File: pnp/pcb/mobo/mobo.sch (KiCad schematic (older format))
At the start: 21 parts, among them J5 Conn_ARM_JTAG_SWD_10, SW2 RESET, U1 STM32F407VETx, Y1 12MHz, Y3 32.768MHz

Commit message: decided to stick with original layout. added footprint and schematic for 2SMPP-03 vacuum sensor
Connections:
- net labels removed: MOTOR_CIPO, MOTOR_COPI, MOTOR_C_CS, MOTOR_P_CS, MOTOR_R_CS, MOTOR_SCK, MOTOR_X_CS, MOTOR_Y_CS, MOTOR_Z_CS
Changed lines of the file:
@@
 Text GLabel 2200 6600 0    50   Input ~ 0
 485_3_RTS
-Text GLabel 4000 6500 2    50   Input ~ 0
-MOTOR_CIPO
-Text GLabel 4000 6600 2    50   Input ~ 0
-MOTOR_COPI
-Text GLabel 4000 6400 2    50   Input ~ 0
-MOTOR_SCK
-Text GLabel 4000 3500 2    50   Input ~ 0
-MOTOR_X_CS
-Text GLabel 4000 4500 2    50   Input ~ 0
-MOTOR_Y_CS
-Text GLabel 4000 4600 2    50   Input ~ 0
-MOTOR_Z_CS
-Text GLabel 4000 5800 2    50   Input ~ 0
-MOTOR_R_CS
-Text GLabel 4000 5900 2    50   Input ~ 0
-MOTOR_P_CS
-Text GLabel 4000 6000 2    50   Input ~ 0
-MOTOR_C_CS
 $Comp
 L Device:R_Small R1

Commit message: reassigned gpio to make routing easier, did some routing, started working out the schematic for the 2smpp-03
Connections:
- net labels added: C_LIMIT, P_LIMIT, R_LIMIT
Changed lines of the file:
@@
 Text Notes 7000 6650 0    50   ~ 0
 Therm3 -> VAC1\n
-Text GLabel 2200 6100 0    50   Input ~ 0
+Text GLabel 2200 4200 0    50   Input ~ 0
 Z_DIR
-Text GLabel 2200 6000 0    50   Input ~ 0
+Text GLabel 2200 4300 0    50   Input ~ 0
 Z_STEP
-Text GLabel 2200 5800 0    50   Input ~ 0
+Text GLabel 4000 6700 2    50   Input ~ 0
 Z_EN
 Text GLabel 4000 5400 2    50   Input ~ 0
 VAC1_SIG
-Text GLabel 2200 3800 0    50   Input ~ 0
+Text GLabel 2200 6800 0    50   Input ~ 0
 Y_LIMIT
+Text GLabel 4000 4900 2    50   Input ~ 0
+MOSFET4_EN
 Text GLabel 4000 5200 2    50   Input ~ 0
-MOSFET4_EN
-Text GLabel 4000 4900 2    50   Input ~ 0
 MOSFET1_EN
-Text GLabel 4000 5000 2    50   Input ~ 0
+Text GLabel 4000 5100 2    50   Input ~ 0
 MOSFET2_EN
-Text GLabel 2200 4900 0    50   Input ~ 0
+Text GLabel 2200 4800 0    50   Input ~ 0
 SERVO1_SIG
-Text GLabel 2200 4700 0    50   Input ~ 0
+Text GLabel 2200 5400 0    50   Input ~ 0
 Y_DIR
-Text GLabel 2200 4800 0    50   Input ~ 0
+Text GLabel 2200 5500 0    50   Input ~ 0
 Y_STEP
 Text GLabel 4000 5700 2    50   Input ~ 0
@@
 Text GLabel 4000 5500 2    50   Input ~ 0
 VAC2_SIG
-Text GLabel 2200 5000 0    50   Input ~ 0
+Text GLabel 2200 5600 0    50   Input ~ 0
 Y_EN
-Text GLabel 2200 5600 0    50   Input ~ 0
+Text GLabel 2200 6000 0    50   Input ~ 0
 X_DIR
-Text GLabel 2200 5700 0    50   Input ~ 0
+Text GLabel 2200 6100 0    50   Input ~ 0
 X_STEP
-Text GLabel 2200 3700 0    50   Input ~ 0
+Text GLabel 4000 6000 2    50   Input ~ 0
 X_LIMIT
-Text GLabel 2200 6800 0    50   Input ~ 0
+Text GLabel 2200 5800 0    50   Input ~ 0
 C_STEP
-Text GLabel 2200 5200 0    50   Input ~ 0
+Text GLabel 2200 4900 0    50   Input ~ 0
 SERVO2_SIG
-Text GLabel 2200 5400 0    50   Input ~ 0
+Text GLabel 4000 4000 2    50   Input ~ 0
 X_EN
-Text GLabel 2200 5100 0    50   Input ~ 0
+Text GLabel 4000 6300 2    50   Input ~ 0
 Z_LIMIT
 Text GLabel 4000 4800 2    50   Input ~ 0
@@
 Text GLabel 4000 4700 2    50   Input ~ 0
 SCL
-Text GLabel 2200 4000 0    50   Input ~ 0
+Text GLabel 4000 4300 2    50   Input ~ 0
 P_EN
-Text GLabel 2200 4300 0    50   Input ~ 0
+Text GLabel 2200 5000 0    50   Input ~ 0
 DOWNWARDS_LIGHT_SIG
-Text GLabel 2200 4200 0    50   Input ~ 0
+Text GLabel 2200 5100 0    50   Input ~ 0
 UPWARDS_LIGHT_SIG
-Text GLabel 2200 3900 0    50   Input ~ 0
+Text GLabel 4000 4100 2    50   Input ~ 0
 P_DIR
-Text GLabel 2200 6900 0    50   Input ~ 0
+Text GLabel 2200 5700 0    50   Input ~ 0
 C_DIR
-Text GLabel 2200 4100 0    50   Input ~ 0
+Text GLabel 4000 4200 2    50   Input ~ 0
 P_STEP
-Text GLabel 2200 6700 0    50   Input ~ 0
+Text GLabel 2200 5900 0    50   Input ~ 0
 C_EN
-Text GLabel 4000 5100 2    50   Input ~ 0
+Text GLabel 4000 5000 2    50   Input ~ 0
 MOSFET3_EN
 Text GLabel 4000 2600 2    50   Input ~ 0
@@
 Text GLabel 4000 2500 2    50   Input ~ 0
 SCK
-Text GLabel 4000 4300 2    50   Input ~ 0
+Text GLabel 2200 3900 0    50   Input ~ 0
 R_DIR
-Text GLabel 4000 4200 2    50   Input ~ 0
+Text GLabel 2200 4000 0    50   Input ~ 0
 R_STEP
-Text GLabel 4000 4000 2    50   Input ~ 0
+Text GLabel 2200 4100 0    50   Input ~ 0
 R_EN
 $Comp
@@
 Wire Wire Line
 	900  3750 900  3800
+Text GLabel 4000 6200 2    50   Input ~ 0
+R_LIMIT
+Text GLabel 4000 6100 2    50   Input ~ 0
+P_LIMIT
+Text GLabel 2200 6900 0    50   Input ~ 0
+C_LIMIT
 $EndSCHEMATC

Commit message: finished schematics for vacuum sensor, did some more routing for mosfets
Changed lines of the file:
@@
 Text GLabel 4000 5400 2    50   Input ~ 0
 VAC1_SIG
-Text GLabel 2200 6800 0    50   Input ~ 0
+Text GLabel 4000 5000 2    50   Input ~ 0
 Y_LIMIT
-Text GLabel 4000 4900 2    50   Input ~ 0
+Text GLabel 2200 6700 0    50   Input ~ 0
 MOSFET4_EN
-Text GLabel 4000 5200 2    50   Input ~ 0
+Text GLabel 4000 6000 2    50   Input ~ 0
 MOSFET1_EN
-Text GLabel 4000 5100 2    50   Input ~ 0
+Text GLabel 2200 6900 0    50   Input ~ 0
 MOSFET2_EN
 Text GLabel 2200 4800 0    50   Input ~ 0
@@
 Text GLabel 2200 6100 0    50   Input ~ 0
 X_STEP
-Text GLabel 4000 6000 2    50   Input ~ 0
+Text GLabel 4000 5200 2    50   Input ~ 0
 X_LIMIT
 Text GLabel 2200 5800 0    50   Input ~ 0
@@
 Text GLabel 2200 5900 0    50   Input ~ 0
 C_EN
-Text GLabel 4000 5000 2    50   Input ~ 0
+Text GLabel 2200 6800 0    50   Input ~ 0
 MOSFET3_EN
 Text GLabel 4000 2600 2    50   Input ~ 0
@@
 Wire Wire Line
 	2200 2850 2250 2850
-Text GLabel 4000 2900 2    50   Input ~ 0
+Text GLabel 2200 6200 0    50   Input ~ 0
 485_1_RXI
-Text GLabel 4000 3000 2    50   Input ~ 0
+Text GLabel 2200 6300 0    50   Input ~ 0
 485_1_TXO
-Text GLabel 4000 2800 2    50   Input ~ 0
+Text GLabel 2200 6600 0    50   Input ~ 0
 485_1_RTS
 Text GLabel 4000 2200 2    50   Input ~ 0
@@
 Text GLabel 4000 2100 2    50   Input ~ 0
 485_2_RTS
-Text GLabel 2200 6200 0    50   Input ~ 0
+Text GLabel 4000 2900 2    50   Input ~ 0
 485_3_RXI
-Text GLabel 2200 6300 0    50   Input ~ 0
+Text GLabel 4000 3000 2    50   Input ~ 0
 485_3_TXO
-Text GLabel 2200 6600 0    50   Input ~ 0
+Text GLabel 4000 2800 2    50   Input ~ 0
 485_3_RTS
 $Comp
@@
 Text GLabel 4000 6100 2    50   Input ~ 0
 P_LIMIT
-Text GLabel 2200 6900 0    50   Input ~ 0
+Text GLabel 4000 5100 2    50   Input ~ 0
 C_LIMIT
 $EndSCHEMATC

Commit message: cleaned up silkscreens, added version and info text
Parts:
- Y1: symbol Device:Crystal_GND24_Small -> mobo-rescue:Crystal_GND24_Small-Device
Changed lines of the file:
@@
 	5900 2500 5900 2450
 $Comp
-L Device:Crystal_GND24_Small Y1
+L mobo-rescue:Crystal_GND24_Small-Device Y1
 U 1 1 5F20EB5B
 P 900 3600

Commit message: switched to more monolithic vacuum sensor. rerouted for it. routed aux ports. exported and ordered. this commit exactly reflects REV001 hardware.
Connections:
- net labels added: AUX1-A1, AUX1-A2, AUX1-D1, AUX1-D2, AUX2-A1, AUX2-A2, AUX2-D1, AUX2-D2
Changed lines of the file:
@@
 Text GLabel 4000 5100 2    50   Input ~ 0
 C_LIMIT
+Text GLabel 4000 5800 2    50   Input ~ 0
+AUX1-A2
+Text GLabel 4000 5900 2    50   Input ~ 0
+AUX2-A2
+Text GLabel 2200 4600 0    50   Input ~ 0
+AUX1-D1
+Text GLabel 2200 4400 0    50   Input ~ 0
+AUX1-D2
+Text GLabel 2200 4700 0    50   Input ~ 0
+AUX2-D1
+Text GLabel 2200 4500 0    50   Input ~ 0
+AUX2-D2
+Text GLabel 4000 3800 2    50   Input ~ 0
+AUX2-A1
+Text GLabel 4000 3700 2    50   Input ~ 0
+AUX1-A1
 $EndSCHEMATC

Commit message: removed LSE and changed HSE to 8MHz
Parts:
- removed C23, C25: 22pF, Capacitor_SMD:C_0805_2012Metric_Pad1.15x1.40mm_HandSolder, symbol Device:C_Small
- removed Y3: 32.768MHz, Crystal:Crystal_SMD_3215-2Pin_3.2x1.5mm, symbol Device:Crystal_Small
- Y1: value 12MHz -> 8MHz
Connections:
- wire segments 74 -> 64
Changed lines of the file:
@@
 	1850 2750 1850 2700
-$Comp
-L Device:Crystal_Small Y3
-U 1 1 5F0E266F
-P 4400 7050
-F 0 "Y3" H 4400 7275 50  0000 C CNN
-F 1 "32.768MHz" H 4400 7184 50  0000 C CNN
-F 2 "Crystal:Crystal_SMD_3215-2Pin_3.2x1.5mm" H 4400 7050 50  0001 C CNN
-F 3 "~" H 4400 7050 50  0001 C CNN
-	1    4400 7050
-	1    0    0    -1
-$EndComp
-$Comp
-L Device:C_Small C25
-U 1 1 5F0E33A4
-P 4600 7250
-F 0 "C25" H 4692 7296 50  0000 L CNN
-F 1 "22pF" H 4692 7205 50  0000 L CNN
-F 2 "Capacitor_SMD:C_0805_2012Metric_Pad1.15x1.40mm_HandSolder" H 4600 7250 50  0001 C CNN
-F 3 "~" H 4600 7250 50  0001 C CNN
-	1    4600 7250
-	1    0    0    -1
-$EndComp
-$Comp
-L Device:C_Small C23
-U 1 1 5F0E4761
-P 4200 7250
-F 0 "C23" H 4292 7296 50  0000 L CNN
-F 1 "22pF" H 4292 7205 50  0000 L CNN
-F 2 "Capacitor_SMD:C_0805_2012Metric_Pad1.15x1.40mm_HandSolder" H 4200 7250 50  0001 C CNN
-F 3 "~" H 4200 7250 50  0001 C CNN
-	1    4200 7250
-	1    0    0    -1
-$EndComp
-Wire Wire Line
-	4200 7150 4200 7050
-Wire Wire Line
-	4200 7050 4300 7050
-Wire Wire Line
-	4500 7050 4600 7050
-Wire Wire Line
-	4600 7050 4600 7150
-$Comp
-L power:GND #PWR0124
-U 1 1 5F0E65D5
-P 4200 7450
-F 0 "#PWR0124" H 4200 7200 50  0001 C CNN
-F 1 "GND" H 4205 7277 50  0000 C CNN
-F 2 "" H 4200 7450 50  0001 C CNN
-F 3 "" H 4200 7450 50  0001 C CNN
-	1    4200 7450
-	1    0    0    -1
-$EndComp
-$Comp
-L power:GND #PWR0125
-U 1 1 5F0E6A2C
-P 4600 7450
-F 0 "#PWR0125" H 4600 7200 50  0001 C CNN
-F 1 "GND" H 4605 7277 50  0000 C CNN
-F 2 "" H 4600 7450 50  0001 C CNN
-F 3 "" H 4600 7450 50  0001 C CNN
-	1    4600 7450
-	1    0    0    -1
-$EndComp
-Wire Wire Line
-	4600 7450 4600 7350
-Wire Wire Line
-	4200 7450 4200 7350
-Wire Wire Line
-	4200 7050 4200 6900
-Wire Wire Line
-	4200 6900 4000 6900
-Connection ~ 4200 7050
-Wire Wire Line
-	4600 7050 4600 6800
-Wire Wire Line
-	4600 6800 4000 6800
-Connection ~ 4600 7050
 $Comp
 L Device:C_Small C15
@@
 P 900 3600
 F 0 "Y1" H 1044 3646 50  0000 L CNN
-F 1 "12MHz" H 750 3750 50  0000 L CNN
+F 1 "8MHz" H 750 3750 50  0000 L CNN
 F 2 "Crystal:Crystal_SMD_3225-4Pin_3.2x2.5mm" H 900 3600 50  0001 C CNN
 F 3 "~" H 900 3600 50  0001 C CNN

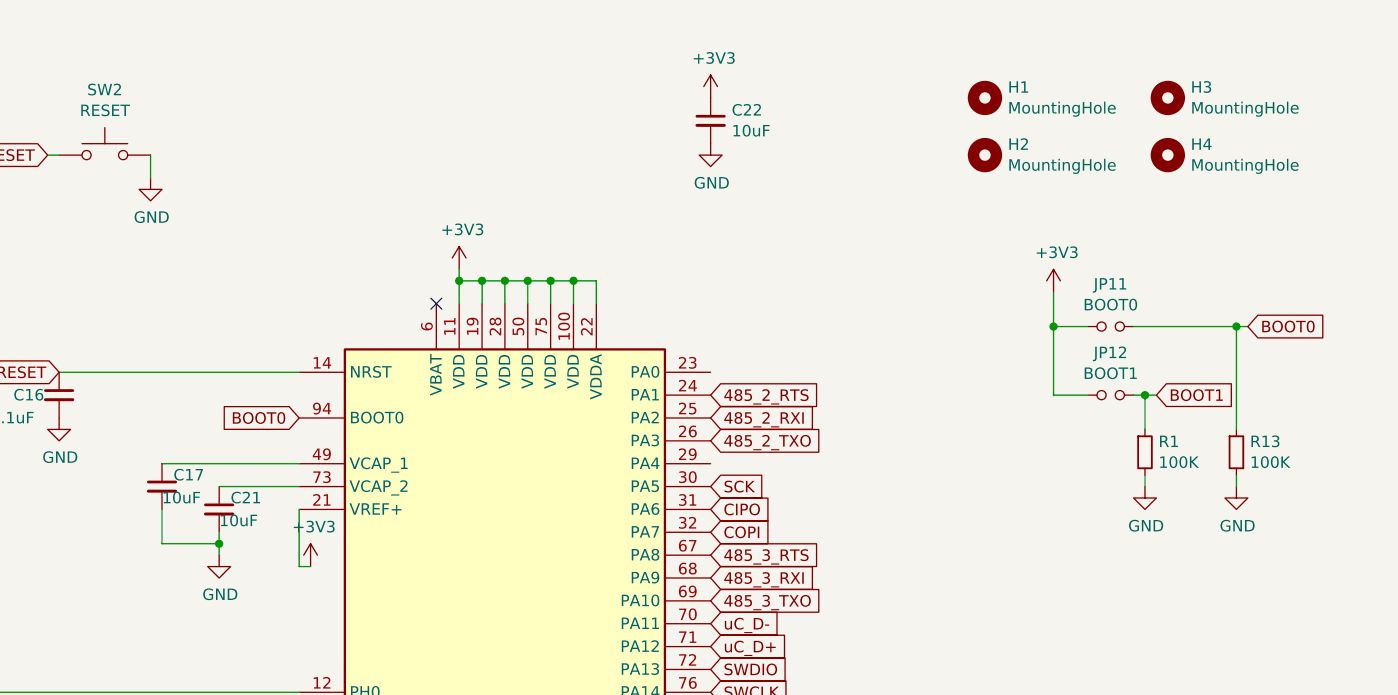
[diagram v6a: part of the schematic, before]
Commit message: fixing decoupling caps based on datasheet and reference design
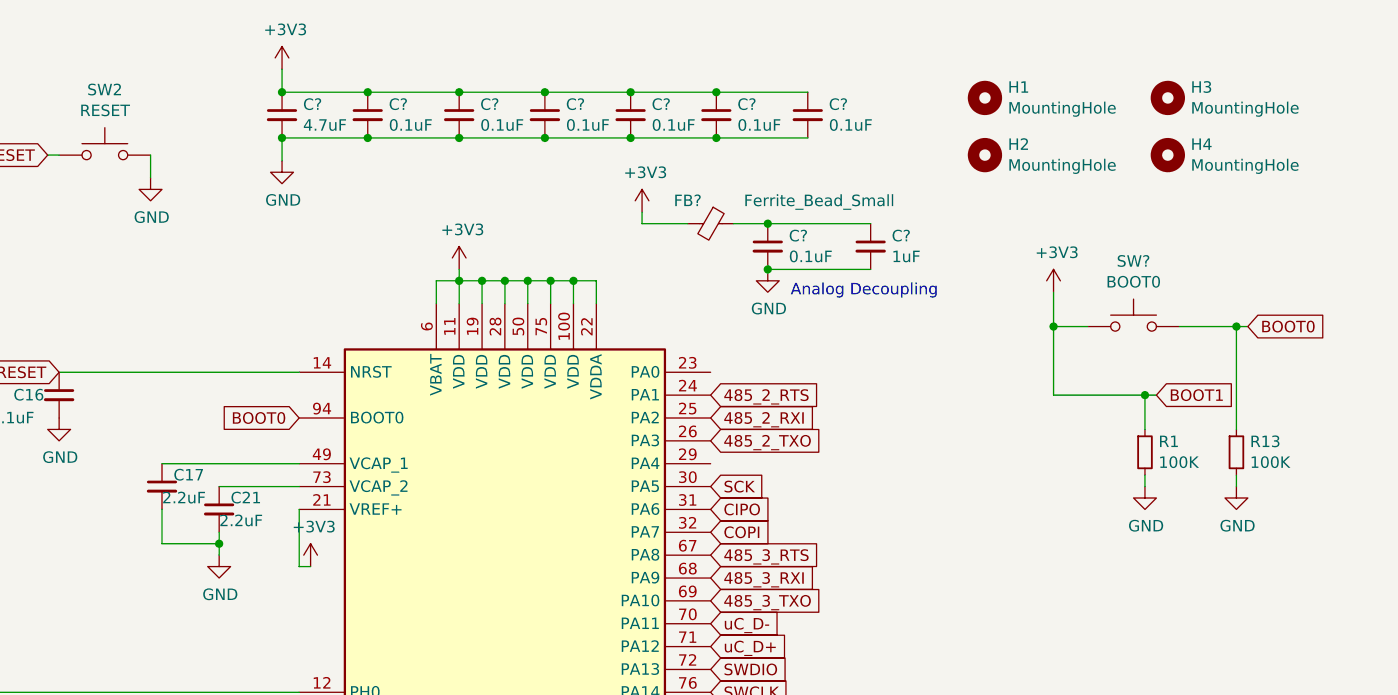
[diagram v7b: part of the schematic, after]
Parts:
- removed C22: 10uF, Capacitor_SMD:C_0805_2012Metric_Pad1.15x1.40mm_HandSolder, symbol Device:C_Small
- removed JP11: BOOT0, Jumper:SolderJumper-2_P1.3mm_Open_RoundedPad1.0x1.5mm, symbol Device:Jumper_NO_Small
- removed JP12: BOOT1, Jumper:SolderJumper-2_P1.3mm_Open_RoundedPad1.0x1.5mm, symbol Device:Jumper_NO_Small
- added C? (x7): 0.1uF, Capacitor_SMD:C_0805_2012Metric_Pad1.15x1.40mm_HandSolder, symbol Device:C_Small
- added C?: 1uF, Capacitor_SMD:C_0805_2012Metric_Pad1.15x1.40mm_HandSolder, symbol Device:C_Small
- added C?: 4.7uF, Capacitor_SMD:C_0805_2012Metric_Pad1.15x1.40mm_HandSolder, symbol Device:C_Small
- added FB?: Ferrite_Bead_Small, symbol Device:Ferrite_Bead_Small
- added SW?: BOOT0, Button_Switch_SMD:SW_SPST_B3S-1000, symbol Switch:SW_Push
- C17, C21: value 10uF -> 2.2uF
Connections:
- net BOOT1 is gone; now on net +3V3: R1.1, U1.37 (PB2)
- net +3V3: now also U1.6 (VBAT), C?.1, C?.1, C?.1, C?.1, C?.1, C?.1, C?.1, FB?.2, SW?.1
- net BOOT0: now also SW?.2
- net GND: now also C?.2, C?.2, C?.2, C?.2, C?.2, C?.2, C?.2, C?.2, C?.2
- new net: C?.1, C?.1, FB?.1
- no-connect marks 1 -> 0
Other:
- note added: "Analog Decoupling"

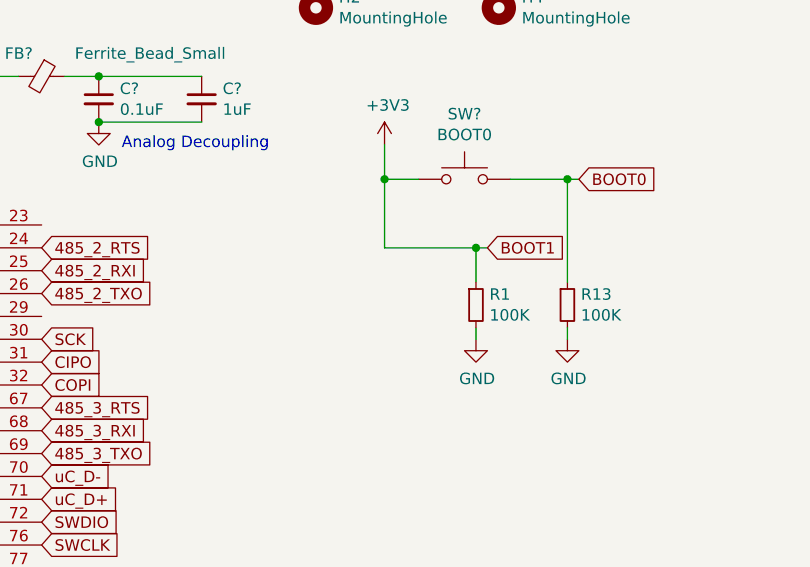
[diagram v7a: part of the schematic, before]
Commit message: updating M0/1/2 pins on stepper driver headers to work for SPI. jumper config not yet finished
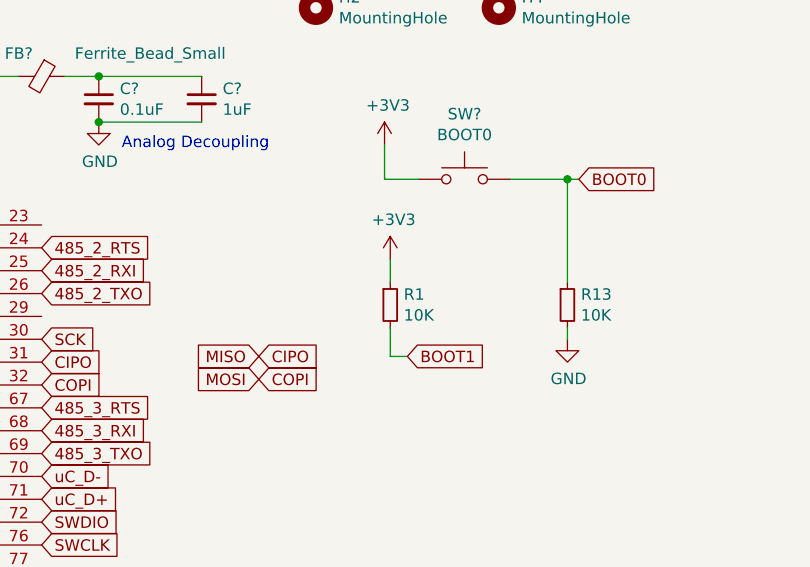
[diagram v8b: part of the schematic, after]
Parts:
- R1, R13: value 100K -> 10K
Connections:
- net +3V3: no longer U1.37 (PB2)
- net GND: no longer R1.2
- new net BOOT1: R1.2, U1.37 (PB2)
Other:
- moved on the sheet: R1
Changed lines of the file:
@@
 L Device:R_Small R1
 U 1 1 5F1837F8
-P 5900 2350
-F 0 "R1" H 5959 2396 50  0000 L CNN
-F 1 "100K" H 5959 2305 50  0000 L CNN
-F 2 "Resistor_SMD:R_0805_2012Metric_Pad1.15x1.40mm_HandSolder" H 5900 2350 50  0001 C CNN
-F 3 "~" H 5900 2350 50  0001 C CNN
-	1    5900 2350
+P 5525 2350
+F 0 "R1" H 5584 2396 50  0000 L CNN
+F 1 "10K" H 5584 2305 50  0000 L CNN
+F 2 "Resistor_SMD:R_0805_2012Metric_Pad1.15x1.40mm_HandSolder" H 5525 2350 50  0001 C CNN
+F 3 "~" H 5525 2350 50  0001 C CNN
+	1    5525 2350
 	1    0    0    -1
 $EndComp
@@
 Text GLabel 4000 3900 2    50   Input ~ 0
 BOOT1
-Text GLabel 5950 2100 2    50   Input ~ 0
+Text GLabel 5600 2575 2    50   Input ~ 0
 BOOT1
 $Comp
@@
 Wire Wire Line
 	5500 1800 5650 1800
-Wire Wire Line
-	5500 1800 5500 2100
-Connection ~ 5500 1800
-Wire Wire Line
-	5900 2250 5900 2100
-Connection ~ 5900 2100
-Wire Wire Line
-	5900 2100 5950 2100
 $Comp
 L Device:R_Small R13
@@
 P 6300 2350
 F 0 "R13" H 6359 2396 50  0000 L CNN
-F 1 "100K" H 6359 2305 50  0000 L CNN
+F 1 "10K" H 6359 2305 50  0000 L CNN
 F 2 "Resistor_SMD:R_0805_2012Metric_Pad1.15x1.40mm_HandSolder" H 6300 2350 50  0001 C CNN
 F 3 "~" H 6300 2350 50  0001 C CNN
@@
 Wire Wire Line
 	6300 1800 6350 1800
-$Comp
-L power:GND #PWR0105
-U 1 1 5F1902E4
-P 5900 2500
-F 0 "#PWR0105" H 5900 2250 50  0001 C CNN
-F 1 "GND" H 5905 2327 50  0000 C CNN
-F 2 "" H 5900 2500 50  0001 C CNN
-F 3 "" H 5900 2500 50  0001 C CNN
-	1    5900 2500
-	1    0    0    -1
-$EndComp
 $Comp
 L power:GND #PWR0107
@@
 Wire Wire Line
 	6300 2500 6300 2450
-Wire Wire Line
-	5900 2500 5900 2450
 $Comp
 L mobo-rescue:Crystal_GND24_Small-Device Y1
@@
 $EndComp
 Wire Wire Line
-	5500 2100 5900 2100
-Wire Wire Line
 	6050 1800 6300 1800
 Connection ~ 6300 1800
@@
 	4025 975  4425 975
 Connection ~ 4025 975
+$Comp
+L power:+3V3 #PWR?
+U 1 1 5F8341E5
+P 5525 2150
+F 0 "#PWR?" H 5525 2000 50  0001 C CNN
+F 1 "+3V3" H 5540 2323 50  0000 C CNN
+F 2 "" H 5525 2150 50  0001 C CNN
+F 3 "" H 5525 2150 50  0001 C CNN
+	1    5525 2150
+	1    0    0    -1
+$EndComp
+Wire Wire Line
+	5525 2150 5525 2250
+Wire Wire Line
+	5525 2450 5525 2575
+Wire Wire Line
+	5525 2575 5600 2575
+Text GLabel 4950 2575 2    50   Input ~ 0
+CIPO
+Text GLabel 4950 2675 2    50   Input ~ 0
+COPI
+Text GLabel 4950 2675 0    50   Input ~ 0
+MOSI
+Text GLabel 4950 2575 0    50   Input ~ 0
+MISO
 $EndSCHEMATC
